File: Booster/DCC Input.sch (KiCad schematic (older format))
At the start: 8 parts

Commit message: Fixed pull down to the required pull-up on the 6N137.
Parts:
- U?: symbol 6N136 -> 6N136-RESCUE-Booster
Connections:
- wire segments 28 -> 26
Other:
- moved on the sheet: R?
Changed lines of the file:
@@
 EESchema Schematic File Version 2
+LIBS:Booster-rescue
 LIBS:Trainiot
 LIBS:power
@@
 $EndDescr
 $Comp
-L 6N136 U?
+L 6N136-RESCUE-Booster U?
 U 1 1 59E8F220
 P 5600 4450
+AR Path="/59E8F220" Ref="U?"  Part="1"
+AR Path="/59E8EF77/59E8F220" Ref="U?"  Part="1"
 F 0 "U?" H 5400 4750 50  0000 L CNN
 F 1 "6N136" H 5600 4750 50  0000 L CNN
@@
 	6100 4350 6100 4250
 Connection ~ 6100 4250
-Wire Wire Line
-	5900 4550 8100 4550
 $Comp
 L GND #PWR?
@@
 L R R?
 U 1 1 59E8F277
-P 7000 5100
-F 0 "R?" V 7080 5100 50  0000 C CNN
-F 1 "10K" V 7000 5100 50  0000 C CNN
-F 2 "" V 6930 5100 50  0001 C CNN
-F 3 "" H 7000 5100 50  0001 C CNN
-	1    7000 5100
-	1    0    0    -1
-$EndComp
-Wire Wire Line
-	7000 4950 7000 4550
-Connection ~ 7000 4550
-$Comp
-L GND #PWR?
-U 1 1 59E8F280
-P 7000 5400
-F 0 "#PWR?" H 7000 5150 50  0001 C CNN
-F 1 "GND" H 7000 5250 50  0000 C CNN
-F 2 "" H 7000 5400 50  0001 C CNN
-F 3 "" H 7000 5400 50  0001 C CNN
-	1    7000 5400
-	1    0    0    -1
-$EndComp
-Wire Wire Line
-	7000 5400 7000 5250
+P 7000 4400
+F 0 "R?" V 7080 4400 50  0000 C CNN
+F 1 "10K" V 7000 4400 50  0000 C CNN
+F 2 "" V 6930 4400 50  0001 C CNN
+F 3 "" H 7000 4400 50  0001 C CNN
+	1    7000 4400
+	1    0    0    -1
+$EndComp
 Wire Wire Line
 	2350 3900 4200 3900
@@
 	1    0    0    -1
 $EndComp
+Wire Wire Line
+	5900 4550 8100 4550
+Connection ~ 7000 4550
 $EndSCHEMATC

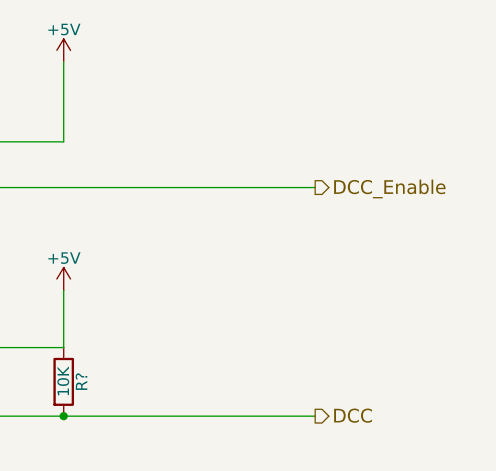
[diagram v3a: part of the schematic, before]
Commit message: Added reversing support. Working on status output.
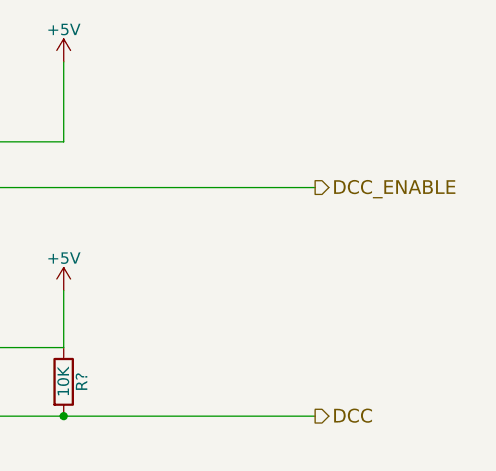
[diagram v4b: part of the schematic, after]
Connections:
- net DCC_Enable renamed DCC_ENABLE
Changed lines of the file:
@@
 $Descr A4 11693 8268
 encoding utf-8
-Sheet 2 6
+Sheet 2 7
 Title "Trainiot Booster"
 Date ""
@@
 DCC
 Text HLabel 8100 3550 2    60   Output ~ 0
-DCC_Enable
+DCC_ENABLE
 $Comp
 L +5V #PWR?

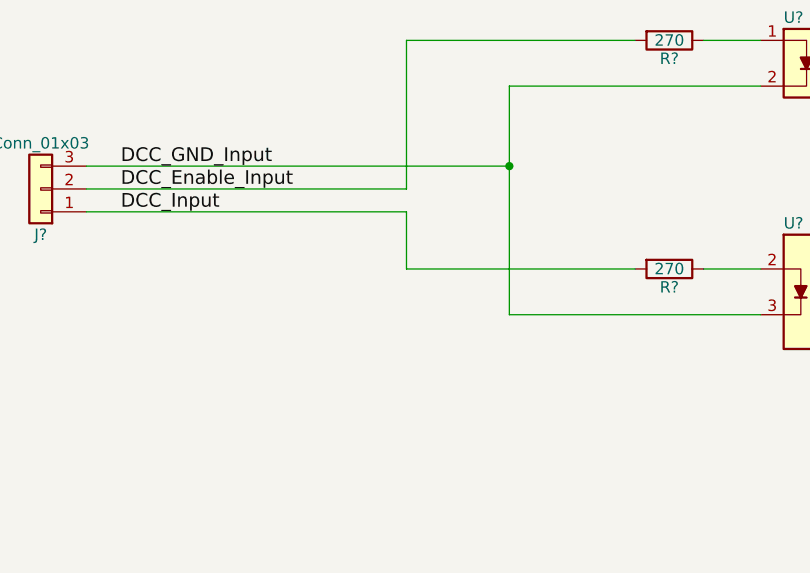
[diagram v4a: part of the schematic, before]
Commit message: Added meassurement tabs and other general "finalizing touches"
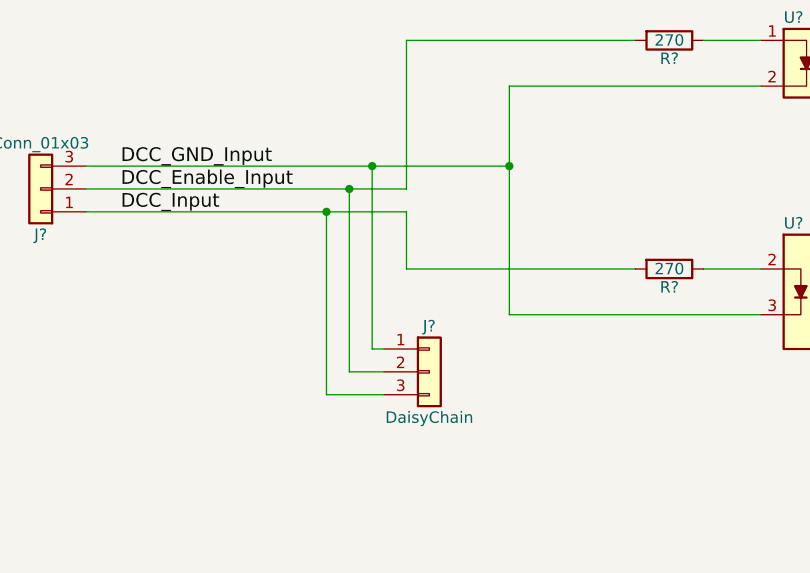
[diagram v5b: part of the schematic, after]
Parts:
- added J?: DaisyChain, symbol Conn_01x03
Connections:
- net DCC_Enable_Input: now also J?.2 (Pin_2)
- net DCC_GND_Input: now also J?.1 (Pin_1)
- net DCC_Input: now also J?.3 (Pin_3)
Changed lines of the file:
@@
 	5900 4550 8100 4550
 Connection ~ 7000 4550
+$Comp
+L Conn_01x03 J?
+U 1 1 5A10589A
+P 3850 4800
+F 0 "J?" H 3850 5000 50  0000 C CNN
+F 1 "DaisyChain" H 3850 4600 50  0000 C CNN
+F 2 "" H 3850 4800 50  0001 C CNN
+F 3 "" H 3850 4800 50  0001 C CNN
+	1    3850 4800
+	1    0    0    -1
+$EndComp
+Wire Wire Line
+	3650 4700 3600 4700
+Wire Wire Line
+	3600 4700 3600 3900
+Connection ~ 3600 3900
+Wire Wire Line
+	3500 4800 3650 4800
+Wire Wire Line
+	3400 4100 3400 4900
+Wire Wire Line
+	3400 4900 3650 4900
+Connection ~ 3400 4100
+Wire Wire Line
+	3500 4000 3500 4800
+Connection ~ 3500 4000
 $EndSCHEMATC

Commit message: Removed need for enable signal replacing it with a missing pulse detection RC based circuit.
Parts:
- removed J?: Conn_01x03, symbol Conn_01x03
- removed J?: DaisyChain, symbol Conn_01x03
- removed R?: 270, symbol R
- removed R?: 10K, symbol R
- removed U?: PC817, Housings_DIP:DIP-4_W7.62mm, symbol PC817
- added C?: 100nF, symbol C
- added D?: D, symbol D
- added P? (x2): CONN_01X02, symbol CONN_01X02
- added R?: 18K, symbol R
- added R? (x3): 10K, symbol R
- added SW?: FORCE_ENABLE, symbol SW_SPST_x03
- added U?: LM339, symbol LM339
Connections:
- net labels added: REF_1.43V
- net labels removed: DCC_Enable_Input
- wire segments 32 -> 50
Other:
- moved on the sheet: C?, R?, U?

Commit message: Fixed missing connections.
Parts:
- gave numbers to parts that had none: 14
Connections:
- wire segments 50 -> 36
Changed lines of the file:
@@
 $EndDescr
 $Comp
-L 6N136-RESCUE-Booster U?
+L 6N136-RESCUE-Booster U201
 U 1 1 59E8F220
 P 4850 4450
-AR Path="/59E8F220" Ref="U?"  Part="1"
-AR Path="/59E8EF77/59E8F220" Ref="U?"  Part="1"
-F 0 "U?" H 4650 4750 50  0000 L CNN
+F 0 "U201" H 4650 4750 50  0000 L CNN
 F 1 "6N136" H 4850 4750 50  0000 L CNN
 F 2 "Housings_DIP:DIP-8_W7.62mm" H 4650 4150 50  0001 L CIN
@@
 $EndComp
 $Comp
-L R R?
+L R R201
 U 1 1 59E8F235
 P 4150 4350
-F 0 "R?" V 4230 4350 50  0000 C CNN
+F 0 "R201" V 4230 4350 50  0000 C CNN
 F 1 "270" V 4150 4350 50  0000 C CNN
 F 2 "" V 4080 4350 50  0001 C CNN
@@
 	4300 4350 4550 4350
 Wire Wire Line
-	1550 4350 2650 4350
-Wire Wire Line
-	2650 4350 4000 4350
+	1550 4350 4000 4350
 Wire Wire Line
 	3450 4550 4550 4550
 Wire Wire Line
-	5150 4250 5350 4250
-Wire Wire Line
-	5350 4250 5650 4250
-Wire Wire Line
-	5650 4250 6250 4250
-$Comp
-L C C?
+	5150 4250 6250 4250
+$Comp
+L C C201
 U 1 1 59E8F24E
 P 5650 4950
-F 0 "C?" H 5675 5050 50  0000 L CNN
+F 0 "C201" H 5675 5050 50  0000 L CNN
 F 1 "100nF" H 5675 4850 50  0000 L CNN
 F 2 "" H 5688 4800 50  0001 C CNN
@@
 Connection ~ 5650 4250
 Wire Wire Line
-	5650 5100 5650 5150
-Wire Wire Line
-	5650 5150 5650 5400
-Wire Wire Line
-	5150 4650 5300 4650
-Wire Wire Line
-	5300 4650 6900 4650
-Wire Wire Line
-	6900 4650 9250 4650
+	5650 5100 5650 5400
+Wire Wire Line
+	5150 4650 9250 4650
 Wire Wire Line
 	5300 5150 5650 5150
@@
 	5150 4350 5350 4350
 Wire Wire Line
-	5350 4250 5350 4350
-Wire Wire Line
-	5350 4350 5350 4550
+	5350 4250 5350 4550
 Connection ~ 5350 4250
 $Comp
-L GND #PWR?
+L GND #PWR01
 U 1 1 59E8F260
 P 5650 5400
-F 0 "#PWR?" H 5650 5150 50  0001 C CNN
+F 0 "#PWR01" H 5650 5150 50  0001 C CNN
 F 1 "GND" H 5650 5250 50  0000 C CNN
 F 2 "" H 5650 5400 50  0001 C CNN
@@
 $EndComp
 $Comp
-L R R?
+L R R202
 U 1 1 59E8F277
 P 5300 4900
-F 0 "R?" V 5380 4900 50  0000 C CNN
+F 0 "R202" V 5380 4900 50  0000 C CNN
 F 1 "10K" V 5300 4900 50  0000 C CNN
 F 2 "" V 5230 4900 50  0001 C CNN
@@
 $EndComp
 Wire Wire Line
-	1550 4450 2850 4450
-Wire Wire Line
-	2850 4450 3450 4450
+	1550 4450 3450 4450
 Text Label 1650 4350 0    60   ~ 0
 DCC_GND_Input
@@
 DCC_ENABLE
 $Comp
-L +5V #PWR?
+L +5V #PWR02
 U 1 1 59E8F78D
 P 6250 4000
-F 0 "#PWR?" H 6250 3850 50  0001 C CNN
+F 0 "#PWR02" H 6250 3850 50  0001 C CNN
 F 1 "+5V" H 6250 4140 50  0000 C CNN
 F 2 "" H 6250 4000 50  0001 C CNN
@@
 	6250 4250 6250 4000
 $Comp
-L +5V #PWR?
+L +5V #PWR03
 U 1 1 59E8F877
 P 7550 2900
-F 0 "#PWR?" H 7550 2750 50  0001 C CNN
+F 0 "#PWR03" H 7550 2750 50  0001 C CNN
 F 1 "+5V" H 7550 3040 50  0000 C CNN
 F 2 "" H 7550 2900 50  0001 C CNN
@@
 Connection ~ 2650 4350
 $Comp
-L D D?
+L D D201
 U 1 1 5A383862
 P 6900 4150
-F 0 "D?" H 6900 4250 50  0000 C CNN
+F 0 "D201" H 6900 4250 50  0000 C CNN
 F 1 "D" H 6900 4050 50  0000 C CNN
 F 2 "" H 6900 4150 50  0000 C CNN
@@
 $EndComp
 Wire Wire Line
-	6900 3250 6900 3500
-Wire Wire Line
-	6900 3500 6900 4000
-$Comp
-L C C?
+	6900 3250 6900 4000
+$Comp
+L C C202
 U 1 1 5A3839FB
 P 7150 3850
-F 0 "C?" H 7175 3950 50  0000 L CNN
+F 0 "C202" H 7175 3950 50  0000 L CNN
 F 1 "100nF" H 7175 3750 50  0000 L CNN
 F 2 "" H 7188 3700 50  0000 C CNN
@@
 $EndComp
 Wire Wire Line
-	6600 3500 6900 3500
-Wire Wire Line
-	6900 3500 7150 3500
-Wire Wire Line
-	7150 3500 8550 3500
-Wire Wire Line
-	7150 4000 7150 4200
-Wire Wire Line
-	7150 4200 7150 4350
-$Comp
-L GND #PWR?
+	6600 3500 8550 3500
+Wire Wire Line
+	7150 4000 7150 4350
+$Comp
+L GND #PWR04
 U 1 1 5A383AD2
 P 7150 4350
-F 0 "#PWR?" H 7150 4100 50  0001 C CNN
+F 0 "#PWR04" H 7150 4100 50  0001 C CNN
 F 1 "GND" H 7150 4200 50  0000 C CNN
 F 2 "" H 7150 4350 50  0000 C CNN
@@
 	3450 4450 3450 4550
 $Comp
-L LM339 U?
-U 2 1 5A38E473
+L LM339 U202
+U 1 1 5A38E473
 P 8850 3600
-F 0 "U?" H 8850 3800 50  0000 L CNN
+F 0 "U202" H 8850 3800 50  0000 L CNN
 F 1 "LM339" H 8850 3400 50  0000 L CNN
 F 2 "" H 8800 3700 50  0000 C CNN
 F 3 "" H 8900 3800 50  0000 C CNN
-	2    8850 3600
-	1    0    0    -1
-$EndComp
-$Comp
-L R R?
+	1    8850 3600
+	1    0    0    -1
+$EndComp
+$Comp
+L R R204
 U 1 1 5A38E517
 P 7550 3150
-F 0 "R?" V 7630 3150 50  0000 C CNN
+F 0 "R204" V 7630 3150 50  0000 C CNN
 F 1 "18K" V 7550 3150 50  0000 C CNN
 F 2 "" V 7480 3150 50  0000 C CNN
@@
 $EndComp
 $Comp
-L R R?
+L R R205
 U 1 1 5A38E55E
 P 7550 3950
-F 0 "R?" V 7630 3950 50  0000 C CNN
+F 0 "R205" V 7630 3950 50  0000 C CNN
 F 1 "10K" V 7550 3950 50  0000 C CNN
 F 2 "" V 7480 3950 50  0000 C CNN
@@
 	7150 3500 7150 3700
 Wire Wire Line
-	7550 3300 7550 3700
-Wire Wire Line
-	7550 3700 7550 3800
+	7550 3300 7550 3800
 Wire Wire Line
 	7550 3700 8550 3700
 Connection ~ 7550 3700
 $Comp
-L R R?
+L R R203
 U 1 1 5A38E85E
 P 6600 3950
-F 0 "R?" V 6680 3950 50  0000 C CNN
+F 0 "R203" V 6680 3950 50  0000 C CNN
 F 1 "10K" V 6600 3950 50  0000 C CNN
 F 2 "" V 6530 3950 50  0000 C CNN
@@
 	6600 4100 6600 4250
 $Comp
-L GND #PWR?
+L GND #PWR05
 U 1 1 5A38E8FE
-P 6600 4300
-F 0 "#PWR?" H 6600 4050 50  0001 C CNN
-F 1 "GND" H 6600 4150 50  0000 C CNN
-F 2 "" H 6600 4300 50  0000 C CNN
-F 3 "" H 6600 4300 50  0000 C CNN
-	1    6600 4300
+P 6600 4250
+F 0 "#PWR05" H 6600 4000 50  0001 C CNN
+F 1 "GND" H 6600 4100 50  0000 C CNN
+F 2 "" H 6600 4250 50  0000 C CNN
+F 3 "" H 6600 4250 50  0000 C CNN
+	1    6600 4250
 	1    0    0    -1
 $EndComp
@@
 Connection ~ 6900 3500
 Wire Wire Line
-	9050 3600 9150 3600
-Wire Wire Line
-	9150 3600 9300 3600
+	9050 3600 9300 3600
 Wire Wire Line
 	9150 3600 9150 3200
 Connection ~ 9150 3600
 $Comp
-L R R?
+L R R206
 U 1 1 5A38EA64
 P 9150 3050
-F 0 "R?" V 9230 3050 50  0000 C CNN
+F 0 "R206" V 9230 3050 50  0000 C CNN
 F 1 "10K" V 9150 3050 50  0000 C CNN
 F 2 "" V 9080 3050 50  0000 C CNN
@@
 	9150 2900 9150 2700
 $Comp
-L +5V #PWR?
+L +5V #PWR06
 U 1 1 5A38EB05
 P 9150 2700
-F 0 "#PWR?" H 9150 2550 50  0001 C CNN
+F 0 "#PWR06" H 9150 2550 50  0001 C CNN
 F 1 "+5V" H 9150 2840 50  0000 C CNN
 F 2 "" H 9150 2700 50  0001 C CNN
@@
 REF_1.43V
 $Comp
-L SW_SPST_x03 SW?
-U 2 1 5A38F800
+L SW_SPST_x03 SW201
+U 1 1 5A38F800
 P 6900 3050
-F 0 "SW?" H 6900 3175 50  0000 C CNN
+F 0 "SW201" H 6900 3175 50  0000 C CNN
 F 1 "FORCE_ENABLE" H 6900 2950 50  0000 C CNN
 F 2 "" H 6900 3050 50  0001 C CNN
 F 3 "" H 6900 3050 50  0001 C CNN
-	2    6900 3050
+	1    6900 3050
 	0    1    1    0
 $EndComp
@@
 	6900 2850 6900 2700
 $Comp
-L +5V #PWR?
+L +5V #PWR07
 U 1 1 5A38FAC1
 P 6900 2700
-F 0 "#PWR?" H 6900 2550 50  0001 C CNN
+F 0 "#PWR07" H 6900 2550 50  0001 C CNN
 F 1 "+5V" H 6900 2840 50  0000 C CNN
 F 2 "" H 6900 2700 50  0001 C CNN
@@
 $EndComp
 $Comp
-L CONN_01X02 P?
+L CONN_01X02 P202
 U 1 1 5A39234E
 P 3100 4850
-F 0 "P?" H 3100 5000 50  0000 C CNN
+F 0 "P202" H 3100 5000 50  0000 C CNN
 F 1 "CONN_01X02" V 3200 4850 50  0000 C CNN
 F 2 "" H 3100 4850 50  0000 C CNN
@@
 $EndComp
 $Comp
-L CONN_01X02 P?
+L CONN_01X02 P201
 U 1 1 5A39248A
 P 1350 4400
-F 0 "P?" H 1350 4550 50  0000 C CNN
+F 0 "P201" H 1350 4550 50  0000 C CNN
 F 1 "CONN_01X02" V 1450 4400 50  0000 C CNN
 F 2 "" H 1350 4400 50  0000 C CNN

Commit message: Fixed optocoupler circuit - had been reading the wrong datasheet :) Still need to invert the pulse detector op amp and adjust reference voltage as the optocoupler inverse the signal.
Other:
- note added: "SWAP and change reference!!!! DCC is low on signal!"
- moved on the sheet: C201, C202, D201, R202, R203, R204, R205, R206, U202A
